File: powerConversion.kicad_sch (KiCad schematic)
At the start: 42 parts, among them IC14 LM5176PWPR, Q10 BSZ067N06LS3_G, Q11 BSZ067N06LS3_G, Q12 BSZ067N06LS3_G, Q13 BSZ067N06LS3_G

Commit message: updated the schematic to remove connection to rocksat, linked schmatic symbols to footprints
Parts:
- C14, C25, C26, C28, C29, C30, C31, C33, C34: footprint (none) -> Capacitor_SMD:C_0402_1005Metric
- C15, C16, C17, C18, C19, C20, C21, C22, C23, C24, C27: footprint (none) -> Capacitor_SMD:C_0603_1608Metric
- D4, D6, D7: footprint DIOM5225X250N -> HEDGE2:CDBA240LL-HF
- IC14: footprint SOP65P640X120-29N -> HEDGE2:LM5176PWPR
- L3: footprint INDPM7066X300N -> HEDGE2:0630CDMCDDS-1R2MC
- Q10, Q11, Q12, Q13: footprint BSZ067N06LS3G -> HEDGE2:BSZ067N06LS3G
- R17, R18, R19, R2, R20, R21, R22, R23, R24, R25, R26, R27, R28: footprint (none) -> Resistor_SMD:R_0402_1005Metric
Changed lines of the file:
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@@
 			)
 		)
-		(property "Footprint" ""
+		(property "Footprint" "Capacitor_SMD:C_0603_1608Metric"
 			(at 226.06 39.37 0)
 			(effects
@@
 			)
 		)
-		(property "Footprint" ""
+		(property "Footprint" "Capacitor_SMD:C_0603_1608Metric"
 			(at 234.95 39.37 0)
 			(effects
@@
 			)
 		)
-		(property "Footprint" "DIOM5225X250N"
+		(property "Footprint" "HEDGE2:CDBA240LL-HF"
 			(at 277.8 102.87 0)
 			(effects
@@
 			)
 		)
-		(property "Footprint" ""
+		(property "Footprint" "Resistor_SMD:R_0402_1005Metric"
 			(at 35.56 121.92 0)
 			(effects
@@
 			)
 		)
-		(property "Footprint" ""
+		(property "Footprint" "Capacitor_SMD:C_0402_1005Metric"
 			(at 55.88 121.92 0)
 			(effects
@@
 			)
 		)
-		(property "Footprint" ""
+		(property "Footprint" "Resistor_SMD:R_0402_1005Metric"
 			(at 46.99 121.92 0)
 			(effects
@@
 			)
 		)
-		(property "Footprint" "INDPM7066X300N"
+		(property "Footprint" "HEDGE2:0630CDMCDDS-1R2MC"
 			(at 173.99 157.15 0)
 			(effects
@@
 			)
 		)
-		(property "Footprint" ""
+		(property "Footprint" "Resistor_SMD:R_0402_1005Metric"
 			(at 76.2 129.54 0)
 			(effects
@@
 			)
 		)
-		(property "Footprint" ""
+		(property "Footprint" "Capacitor_SMD:C_0603_1608Metric"
 			(at 267.97 39.37 0)
 			(effects
@@
 			)
 		)
-		(property "Footprint" ""
+		(property "Footprint" "Capacitor_SMD:C_0402_1005Metric"
 			(at 170.18 95.25 0)
 			(effects
@@
 			)
 		)
-		(property "Footprint" ""
+		(property "Footprint" "Capacitor_SMD:C_0603_1608Metric"
 			(at 45.72 39.37 0)
 			(effects
@@
 			)
 		)
-		(property "Footprint" ""
+		(property "Footprint" "Capacitor_SMD:C_0402_1005Metric"
 			(at 86.36 121.92 0)
 			(effects
@@
 			)
 		)
-		(property "Footprint" ""
+		(property "Footprint" "Capacitor_SMD:C_0402_1005Metric"
 			(at 180.34 119.38 0)
 			(effects
@@
 			)
 		)
-		(property "Footprint" ""
+		(property "Footprint" "Resistor_SMD:R_0402_1005Metric"
 			(at 77.47 57.15 0)
 			(effects
@@
 			)
 		)
-		(property "Footprint" ""
+		(property "Footprint" "Resistor_SMD:R_0402_1005Metric"
 			(at 106.68 57.15 0)
 			(effects
@@
 			)
 		)
-		(property "Footprint" ""
+		(property "Footprint" "Capacitor_SMD:C_0603_1608Metric"
 			(at 58.42 39.37 0)
 			(effects
@@
 			)
 		)
-		(property "Footprint" ""
+		(property "Footprint" "Capacitor_SMD:C_0603_1608Metric"
 			(at 27.94 39.37 0)
 			(effects
@@
 			)
 		)
-		(property "Footprint" "BSZ067N06LS3G"
+		(property "Footprint" "HEDGE2:BSZ067N06LS3G"
 			(at 203.2 162.23 0)
 			(effects
@@
 			)
 		)
-		(property "Footprint" "BSZ067N06LS3G"
+		(property "Footprint" "HEDGE2:BSZ067N06LS3G"
 			(at 149.86 139.37 0)
 			(effects
@@
 			)
 		)
-		(property "Footprint" ""
+		(property "Footprint" "Resistor_SMD:R_0402_1005Metric"
 			(at 106.68 40.64 0)
 			(effects
@@
 			)
 		)
-		(property "Footprint" ""
+		(property "Footprint" "Capacitor_SMD:C_0402_1005Metric"
 			(at 156.21 132.08 0)
 			(effects
@@
 			)
 		)
-		(property "Footprint" "SOP65P640X120-29N"
+		(property "Footprint" "HEDGE2:LM5176PWPR"
 			(at 142.24 192.71 0)
 			(effects
@@
 			)
 		)
-		(property "Footprint" "DIOM5225X250N"
+		(property "Footprint" "HEDGE2:CDBA240LL-HF"
 			(at 72.72 111.76 0)
 			(effects
@@
 			)
 		)
-		(property "Footprint" ""
+		(property "Footprint" "Resistor_SMD:R_0402_1005Metric"
 			(at 248.92 48.26 0)
 			(effects
@@
 			)
 		)
-		(property "Footprint" "BSZ067N06LS3G"
+		(property "Footprint" "HEDGE2:BSZ067N06LS3G"
 			(at 149.86 163.5 0)
 			(effects
@@
 			)
 		)
-		(property "Footprint" ""
+		(property "Footprint" "Resistor_SMD:R_0402_1005Metric"
 			(at 248.92 39.37 0)
 			(effects
@@
 			)
 		)
-		(property "Footprint" ""
+		(property "Footprint" "Capacitor_SMD:C_0603_1608Metric"
 			(at 191.77 105.41 0)
 			(effects
@@
 			)
 		)
-		(property "Footprint" ""
+		(property "Footprint" "Resistor_SMD:R_0402_1005Metric"
 			(at 162.56 138.43 0)
 			(effects
@@
 			)
 		)
-		(property "Footprint" ""
+		(property "Footprint" "Capacitor_SMD:C_0603_1608Metric"
 			(at 67.31 39.37 0)
 			(effects
@@
 			)
 		)
-		(property "Footprint" ""
+		(property "Footprint" "Resistor_SMD:R_0402_1005Metric"
 			(at 200.66 106.68 0)
 			(effects
@@
 			)
 		)
-		(property "Footprint" ""
+		(property "Footprint" "Capacitor_SMD:C_0603_1608Metric"
 			(at 257.81 39.37 0)
 			(effects
@@
 			)
 		)
-		(property "Footprint" ""
+		(property "Footprint" "Capacitor_SMD:C_0402_1005Metric"
 			(at 177.8 133.35 0)
 			(effects
@@
 			)
 		)
-		(property "Footprint" ""
+		(property "Footprint" "Capacitor_SMD:C_0402_1005Metric"
 			(at 76.2 121.92 0)
 			(effects
@@
 			)
 		)
-		(property "Footprint" ""
+		(property "Footprint" "Resistor_SMD:R_0402_1005Metric"
 			(at 149.86 138.43 0)
 			(effects
@@
 			)
 		)
-		(property "Footprint" "BSZ067N06LS3G"
+		(property "Footprint" "HEDGE2:BSZ067N06LS3G"
 			(at 203.2 138.1 0)
 			(effects
@@
 			)
 		)
-		(property "Footprint" ""
+		(property "Footprint" "Capacitor_SMD:C_0402_1005Metric"
 			(at 85.09 69.85 0)
 			(effects
@@
 			)
 		)
-		(property "Footprint" ""
+		(property "Footprint" "Resistor_SMD:R_0402_1005Metric"
 			(at 223.52 71.12 0)
 			(effects
@@
 			)
 		)
-		(property "Footprint" ""
+		(property "Footprint" "Capacitor_SMD:C_0402_1005Metric"
 			(at 66.04 121.92 0)
 			(effects
@@
 			)
 		)
-		(property "Footprint" ""
+		(property "Footprint" "Capacitor_SMD:C_0603_1608Metric"
 			(at 36.83 39.37 0)
 			(effects
@@
 			)
 		)
-		(property "Footprint" ""
+		(property "Footprint" "Resistor_SMD:R_0402_1005Metric"
 			(at 85.09 57.15 0)
 			(effects
@@
 			)
 		)
-		(property "Footprint" "DIOM5225X250N"
+		(property "Footprint" "HEDGE2:CDBA240LL-HF"
 			(at 182.55 39.37 0)
 			(effects
@@
 			)
 		)
-		(property "Footprint" ""
+		(property "Footprint" "Capacitor_SMD:C_0603_1608Metric"
 			(at 217.17 39.37 0)
 			(effects

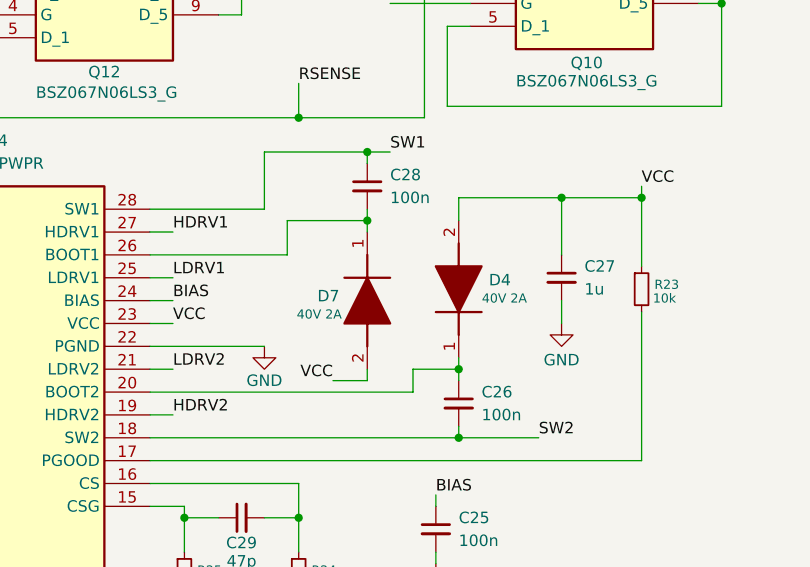
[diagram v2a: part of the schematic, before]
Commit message: Added most 3d models, continued layout
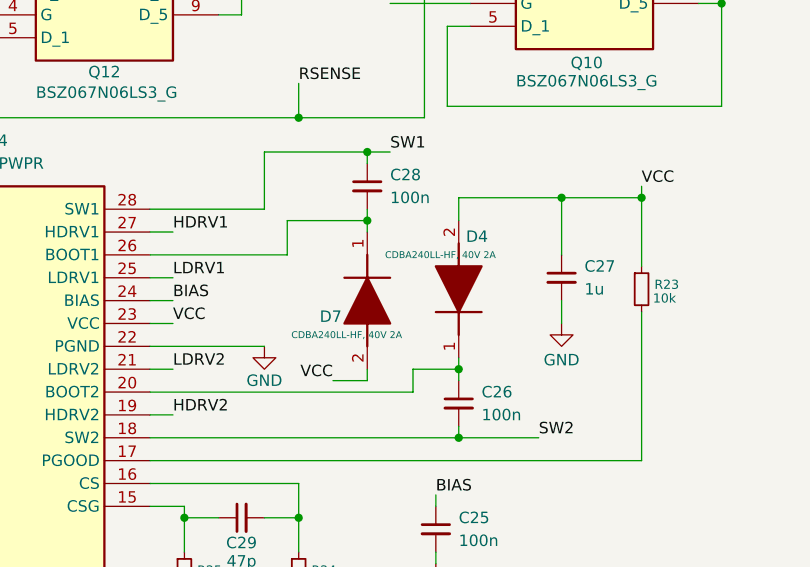
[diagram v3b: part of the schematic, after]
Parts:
- D4, D7: value 40V 2A -> CDBA240LL-HF, 40V 2A
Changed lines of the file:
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@@
 		(dnp no)
 		(property "Reference" "D4"
-			(at 184.912 105.664 90)
-			(effects
-				(font
-					(size 1.27 1.27)
-				)
-			)
-		)
-		(property "Value" "40V 2A"
-			(at 185.42 107.696 90)
-			(effects
-				(font
-					(size 1.016 1.016)
+			(at 182.372 100.838 90)
+			(effects
+				(font
+					(size 1.27 1.27)
+				)
+			)
+		)
+		(property "Value" "CDBA240LL-HF, 40V 2A"
+			(at 178.308 102.87 90)
+			(effects
+				(font
+					(size 0.762 0.762)
 				)
 			)
@@
 		(dnp no)
 		(property "Reference" "D7"
-			(at 165.862 107.442 90)
-			(effects
-				(font
-					(size 1.27 1.27)
-				)
-			)
-		)
-		(property "Value" "40V 2A"
-			(at 164.846 109.474 90)
-			(effects
-				(font
-					(size 1.016 1.016)
-				)
-			)
+			(at 166.116 109.728 90)
+			(effects
+				(font
+					(size 1.27 1.27)
+				)
+			)
+		)
+		(property "Value" "CDBA240LL-HF, 40V 2A"
+			(at 167.894 111.76 90)
+			(effects
+				(font
+					(size 0.762 0.762)
+				)
+			)
